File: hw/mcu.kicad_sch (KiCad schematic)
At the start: 27 parts, among them J100 Conn_01x03_Pin, SW1 SW_Push, SW2 SW_Push, U200 RP2040, U201 W25Q128JVSIQ, X100 ASE-12MHz

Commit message: rerouted
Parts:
- C200, C201, C204, C205, C206, C207, C208, C209, C210, C214: LCSC Part # (none) -> C1525
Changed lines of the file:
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@@
+			)
+		)
+		(property "LCSC Part #" "C1525"
+			(at 142.24 34.29 0)
+			(effects
+				(font
+					(size 1.27 1.27)
+				)
+				(hide yes)
 			)
 		)
@@
 		)
 		(property "Description" "Unpolarized capacitor"
+			(at 66.04 33.02 0)
+			(effects
+				(font
+					(size 1.27 1.27)
+				)
+				(hide yes)
+			)
+		)
+		(property "LCSC Part #" "C1525"
 			(at 66.04 33.02 0)
 			(effects
@@
 			)
 		)
+		(property "LCSC Part #" "C1525"
+			(at 184.15 34.29 0)
+			(effects
+				(font
+					(size 1.27 1.27)
+				)
+				(hide yes)
+			)
+		)
 		(pin "2"
 		)
@@
 			)
 		)
+		(property "LCSC Part #" "C1525"
+			(at 153.67 34.29 0)
+			(effects
+				(font
+					(size 1.27 1.27)
+				)
+				(hide yes)
+			)
+		)
 		(pin "1"
 		)
@@
 		)
 		(property "Description" "Unpolarized capacitor"
+			(at 55.88 33.02 0)
+			(effects
+				(font
+					(size 1.27 1.27)
+				)
+				(hide yes)
+			)
+		)
+		(property "LCSC Part #" "C1525"
 			(at 55.88 33.02 0)
 			(effects
@@
 			)
 		)
+		(property "LCSC Part #" "C1525"
+			(at 130.81 34.29 0)
+			(effects
+				(font
+					(size 1.27 1.27)
+				)
+				(hide yes)
+			)
+		)
 		(pin "1"
 		)
@@
 			)
 		)
+		(property "LCSC Part #" "C1525"
+			(at 163.83 34.29 0)
+			(effects
+				(font
+					(size 1.27 1.27)
+				)
+				(hide yes)
+			)
+		)
 		(pin "2"
 		)
@@
 			)
 		)
+		(property "LCSC Part #" "C1525"
+			(at 173.99 34.29 0)
+			(effects
+				(font
+					(size 1.27 1.27)
+				)
+				(hide yes)
+			)
+		)
 		(pin "2"
 		)
@@
 			)
 		)
+		(property "LCSC Part #" "C1525"
+			(at 199.39 106.68 90)
+			(effects
+				(font
+					(size 1.27 1.27)
+				)
+				(hide yes)
+			)
+		)
 		(pin "2"
 		)
@@
 			(at 194.31 34.29 0)
 			(effects
+				(font
+					(size 1.27 1.27)
+				)
+				(hide yes)
+			)
+		)
+		(property "LCSC Part #" "C1525"
+			(at 194.31 34.29 0)
+			(effects

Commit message: 1p version
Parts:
- removed J100: Conn_01x03_Pin, Connector_PinHeader_2.54mm:PinHeader_1x03_P2.54mm_Vertical, symbol Connector:Conn_01x03_Pin
- removed R205, R206: 27R, Resistor_SMD:R_0402_1005Metric, symbol Device:R
- removed R208: 1k, Resistor_SMD:R_0402_1005Metric, symbol Device:R
- removed SW2: SW_Push, Button_Switch_SMD:SW_SPST_B3U-1000P, symbol Switch:SW_Push
- added J100: Conn_01x05_Pin, Connector_PinHeader_2.54mm:PinHeader_1x05_P2.54mm_Vertical, symbol Connector:Conn_01x05_Pin
- C202, C203, C211: LCSC Part # (none) -> C52923
- U201: value W25Q128JVSIQ -> W25Q16JVUXIQ; footprint Package_SO:SOIC-8_5.23x5.23mm_P1.27mm -> Package_SON:Winbond_USON-8-1EP_3x2mm_P0.5mm_EP0.2x1.6mm; LCSC Part # (none) -> C2843335
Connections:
- net IO2_LEFT is gone; now on net IO_UP: U200.31 (GPIO20)
- net IO2_RIGHT is gone; now on net IO_DOWN: U200.30 (GPIO19)
- net RUN is gone; now on net +3.3V: U200.26 (RUN)
- net USB_DEV_D_N is gone; now on net IO_RIGHT: U200.13 (GPIO10)
- net USB_DEV_D_P is gone; now on net IO_LEFT: U200.14 (GPIO11)
- net GND: now also J100.4 (Pin_4)
- net IO_DOWN: no longer U200.35 (GPIO23)
- net IO_FIRE: now also U200.12 (GPIO9); no longer U200.39 (GPIO27_ADC1)
- net IO_LEFT: no longer U200.37 (GPIO25)
- net IO_RIGHT: no longer U200.38 (GPIO26_ADC0)
- net IO_UP: no longer U200.36 (GPIO24)
- net SWCLK: now also J100.5 (Pin_5)
- net SWD: now also J100.3 (Pin_3)
- net IO2_DOWN renamed UART_RX
- net UART_RX: now also J100.1 (Pin_1)
- net IO2_FIRE: no longer names the net of U200.29 (GPIO18)
- net IO2_UP renamed UART_TX
- net UART_TX: now also J100.2 (Pin_2)
- new net GPIO25: U200.37 (GPIO25)
- no-connect marks 19 -> 23
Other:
- moved on the sheet: C200, C201, C202, C203, C204, C205, C206, C207, C208, C209, C210, C214

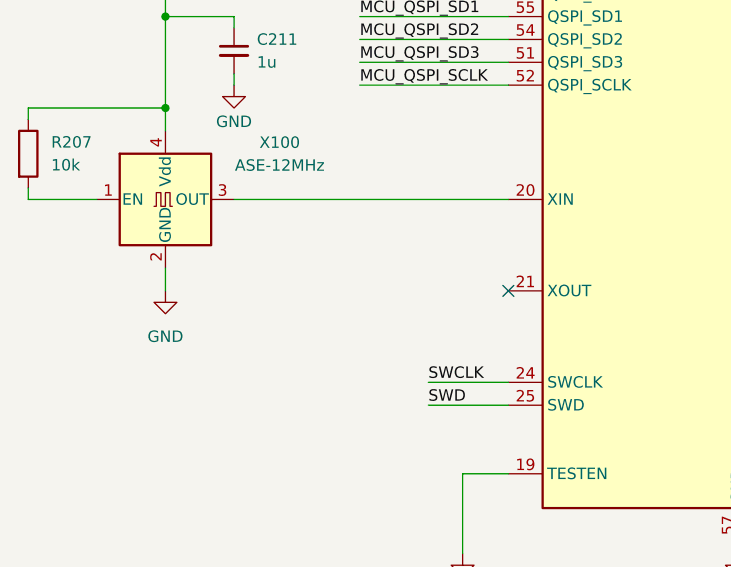
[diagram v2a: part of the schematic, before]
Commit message: added 15pf load capacitor for oscillator
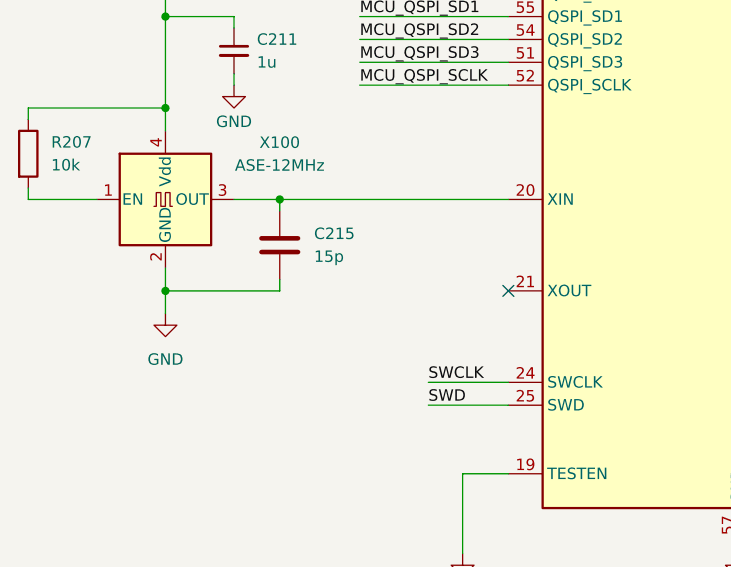
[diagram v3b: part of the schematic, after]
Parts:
- added C215: 15p, Capacitor_SMD:C_0402_1005Metric, symbol Device:C
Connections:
- net GND: now also C215.2
- net at U200.20 (XIN), X100.3 (OUT): now also C215.1
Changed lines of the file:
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@@
 	)
 	(junction
+		(at 35.56 107.95)
+		(diameter 0)
+		(color 0 0 0 0)
+	)
+	(junction
 		(at 189.23 27.94)
 		(diameter 0)
@@
 	)
 	(junction
+		(at 48.26 97.79)
+		(diameter 0)
+		(color 0 0 0 0)
+	)
+	(junction
 		(at 109.22 27.94)
 		(diameter 0)
@@
 	(wire
 		(pts
+			(xy 48.26 107.95) (xy 35.56 107.95)
+		)
+		(stroke
+			(width 0)
+			(type default)
+		)
+	)
+	(wire
+		(pts
 			(xy 124.46 100.33) (xy 125.73 100.33)
 		)
@@
 	(wire
 		(pts
+			(xy 48.26 99.06) (xy 48.26 97.79)
+		)
+		(stroke
+			(width 0)
+			(type default)
+		)
+	)
+	(wire
+		(pts
 			(xy 148.59 27.94) (xy 138.43 27.94)
 		)
@@
 	(wire
 		(pts
+			(xy 48.26 97.79) (xy 73.66 97.79)
+		)
+		(stroke
+			(width 0)
+			(type default)
+		)
+	)
+	(wire
+		(pts
 			(xy 189.23 38.1) (xy 189.23 40.64)
 		)
@@
 	(wire
 		(pts
-			(xy 35.56 105.41) (xy 35.56 107.95)
+			(xy 48.26 106.68) (xy 48.26 107.95)
 		)
 		(stroke
@@
 	(wire
 		(pts
-			(xy 43.18 97.79) (xy 73.66 97.79)
+			(xy 43.18 97.79) (xy 48.26 97.79)
 		)
 		(stroke
@@
 	(wire
 		(pts
+			(xy 35.56 105.41) (xy 35.56 107.95)
+		)
+		(stroke
+			(width 0)
+			(type default)
+		)
+	)
+	(wire
+		(pts
 			(xy 53.34 64.77) (xy 54.61 64.77)
 		)
@@
 	(wire
 		(pts
+			(xy 35.56 107.95) (xy 35.56 110.49)
+		)
+		(stroke
+			(width 0)
+			(type default)
+		)
+	)
+	(wire
+		(pts
 			(xy 124.46 115.57) (xy 125.73 115.57)
 		)
@@
 	(symbol
 		(lib_id "power:GND")
-		(at 35.56 107.95 0)
+		(at 35.56 110.49 0)
 		(unit 1)
 		(exclude_from_sim no)
@@
 		(fields_autoplaced yes)
 		(property "Reference" "#PWR030"
-			(at 35.56 114.3 0)
+			(at 35.56 116.84 0)
 			(effects
 				(font
@@
 		)
 		(property "Value" "GND"
-			(at 35.56 113.03 0)
+			(at 35.56 115.57 0)
 			(effects
 				(font
@@
 		)
 		(property "Footprint" ""
-			(at 35.56 107.95 0)
+			(at 35.56 110.49 0)
 			(effects
 				(font
@@
 		)
 		(property "Datasheet" ""
-			(at 35.56 107.95 0)
+			(at 35.56 110.49 0)
 			(effects
 				(font
@@
 		)
 		(property "Description" "Power symbol creates a global label with name \"GND\" , ground"
-			(at 35.56 107.95 0)
+			(at 35.56 110.49 0)
 			(effects
 				(font
@@
 					(unit 1)
 				)
+			)
+		)
+	)
+	(symbol
+		(lib_id "Device:C")
+		(at 48.26 102.87 0)
+		(unit 1)
+		(exclude_from_sim no)
+		(in_bom yes)
+		(on_board yes)
+		(dnp no)
+		(fields_autoplaced yes)
+		(property "Reference" "C215"
+			(at 52.07 101.5999 0)
+			(effects
+				(font
+					(size 1.27 1.27)
+				)
+				(justify left)
+			)
+		)
+		(property "Value" "15p"
+			(at 52.07 104.1399 0)
+			(effects
+				(font
+					(size 1.27 1.27)
+				)
+				(justify left)
+			)
+		)
+		(property "Footprint" "Capacitor_SMD:C_0402_1005Metric"
+			(at 49.2252 106.68 0)
+			(effects
+				(font
+					(size 1.27 1.27)
+				)
+				(hide yes)
+			)
+		)
+		(property "Datasheet" "~"
+			(at 48.26 102.87 0)
+			(effects
+				(font
+					(size 1.27 1.27)
+				)
+				(hide yes)
+			)
+		)
+		(property "Description" "Unpolarized capacitor"
+			(at 48.26 102.87 0)
+			(effects
+				(font
+					(size 1.27 1.27)
+				)
+				(hide yes)
+			)
+		)
+		(pin "1"
+		)
+		(pin "2"
+		)
+		(instances
+			(project ""
+				(path "/2c829863-8720-4457-b733-fc3614b899de/5f74e6c2-f3af-4c74-8821-80ed6dbd5339"
+					(reference "C215")
+					(unit 1)
+				)

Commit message: pre production review
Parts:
- R203: LCSC Part # (none) -> C11702
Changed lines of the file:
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@@
+			)
+		)
+		(property "LCSC Part #" "C11702"
+			(at 243.84 118.11 90)
+			(effects
+				(font
+					(size 1.27 1.27)
+				)
+				(hide yes)
 			)
 		)

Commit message: production
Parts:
- U200: footprint Package_DFN_QFN:QFN-56-1EP_7x7mm_P0.4mm_EP3.2x3.2mm -> Package_DFN_QFN:QFN-56-1EP_7x7mm_P0.4mm_EP3.2x3.2mm_ThermalVias
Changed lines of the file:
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@@
 			)
 		)
-		(property "Footprint" "Package_DFN_QFN:QFN-56-1EP_7x7mm_P0.4mm_EP3.2x3.2mm"
+		(property "Footprint" "Package_DFN_QFN:QFN-56-1EP_7x7mm_P0.4mm_EP3.2x3.2mm_ThermalVias"
 			(at 99.06 90.17 0)
 			(effects
